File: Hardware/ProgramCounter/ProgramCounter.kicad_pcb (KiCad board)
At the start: 4 copper layers, 25 parts, among them J1 Conn_02x16_Counter_Clockwise, J2 Conn_02x16_Counter_Clockwise

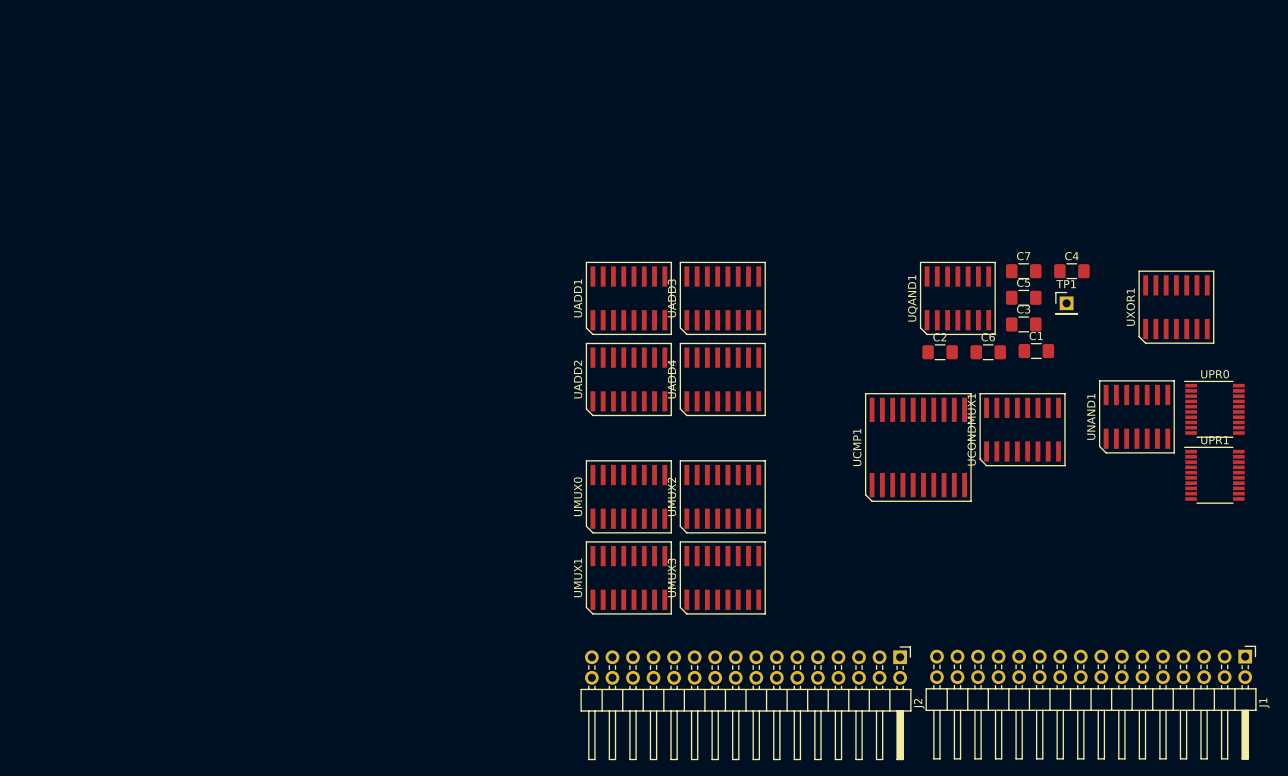
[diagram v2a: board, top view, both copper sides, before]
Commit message: PC Board
Mostly done. Going to move top half down.
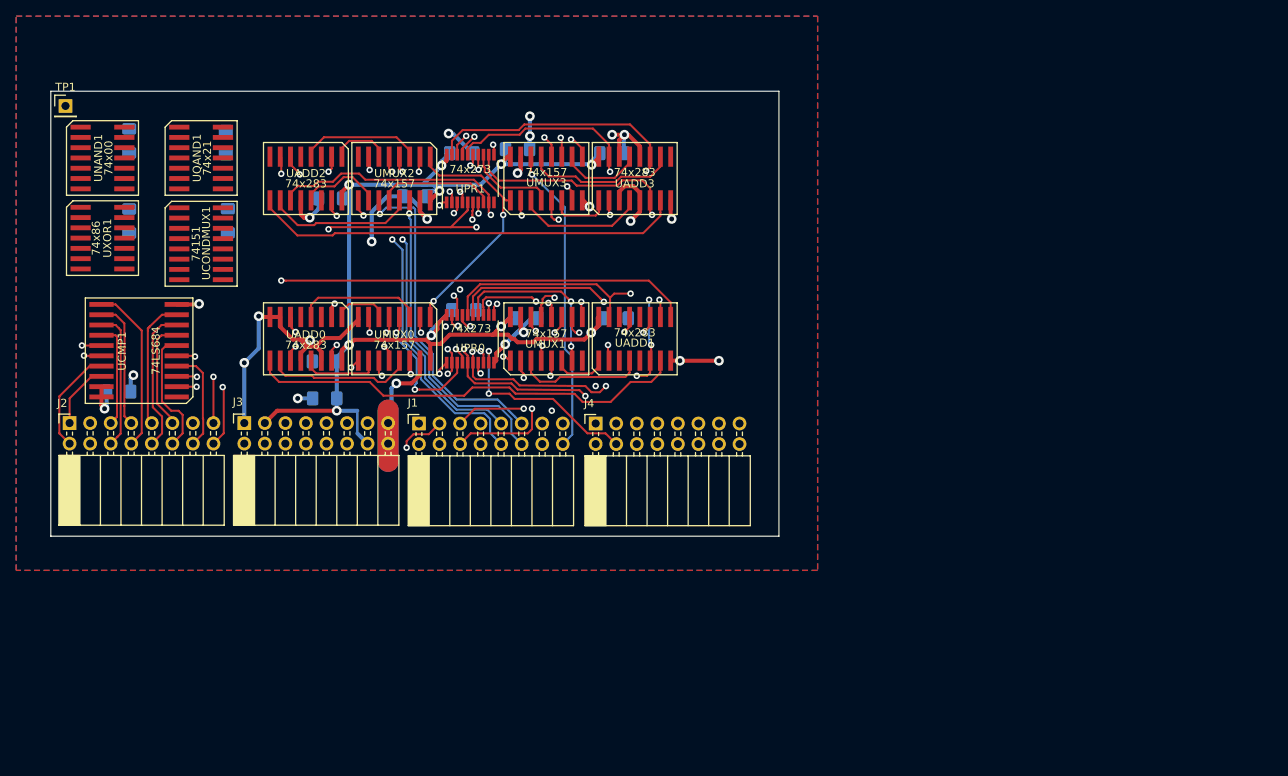
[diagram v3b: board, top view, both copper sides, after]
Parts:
- removed UADD4: 74LS283, aFootprint:R-PDSO-G16
- added C10: .1uF, Capacitor_SMD:C_1206_3216Metric_Pad1.42x1.75mm_HandSolder, B.Cu at (119.3, 57.7)
- added C11: .1uF, Capacitor_SMD:C_1206_3216Metric_Pad1.42x1.75mm_HandSolder, B.Cu at (84.6, 63.2)
- added C12: .1uF, Capacitor_SMD:C_1206_3216Metric_Pad1.42x1.75mm_HandSolder, B.Cu at (71.6, 56.4)
- added C13: .1uF, Capacitor_SMD:C_1206_3216Metric_Pad1.42x1.75mm_HandSolder, B.Cu at (59.7, 66.0)
- added C14: .1uF, Capacitor_SMD:C_1206_3216Metric_Pad1.42x1.75mm_HandSolder, B.Cu at (95.0, 63.0)
- added C15: .1uF, Capacitor_SMD:C_1206_3216Metric_Pad1.42x1.75mm_HandSolder, B.Cu at (107.7, 57.1)
- added C8: .1uF, Capacitor_SMD:C_1206_3216Metric_Pad1.42x1.75mm_HandSolder, B.Cu at (119.9, 78.1)
- added C9: .1uF, Capacitor_SMD:C_1206_3216Metric_Pad1.42x1.75mm_HandSolder, B.Cu at (83.9, 88.0)
- added J3: Conn_02x08, Connector_PinSocket_2.54mm:PinSocket_2x08_P2.54mm_Horizontal, F.Cu at (73.9, 91.0)
- added J4: Conn_02x08, Connector_PinSocket_2.54mm:PinSocket_2x08_P2.54mm_Horizontal, F.Cu at (117.3, 91.1)
- added UADD0: 74x283, aFootprint:R-PDSO-G16, F.Cu at (81.5, 80.6)
- C1, C2, C3, C4, C5, C6, C7: moved to B.Cu
- J1, J2: value Conn_02x16_Counter_Clockwise -> Conn_02x08; footprint Connector_PinHeader_2.54mm:PinHeader_2x16_P2.54mm_Horizontal -> Connector_PinSocket_2.54mm:PinSocket_2x08_P2.54mm_Horizontal
- UADD1, UADD2, UADD3: value 74LS283 -> 74x283
- UMUX0, UMUX1, UMUX2, UMUX3: value 74LS157 -> 74x157
- UNAND1: value 74LS00 -> 74x00
- UPR0, UPR1: value 74HCT273 -> 74x273
- UQAND1: value 74LS21 -> 74x21
- UXOR1: value 74HC86 -> 74x86
- moved UXOR1 133.0 mm to (56.4, 68.2), turned to 270 degrees
- moved UNAND1 131.8 mm to (56.4, 58.2), turned to 270 degrees
- moved TP1 126.1 mm to (51.8, 51.8)
- moved C4 117.6 mm to (59.7, 56.1), turned to 270 degrees
- moved C5 112.5 mm to (58.4, 87.1)
- moved J2 106.7 mm to (52.3, 91.0), turned to 90 degrees
- moved J1 106.1 mm to (95.5, 91.1), turned to 90 degrees
- moved UCONDMUX1 104.1 mm to (68.6, 68.8), turned to 270 degrees
- moved C3 99.2 mm to (71.9, 66.0), turned to 270 degrees
- moved UPR1 99.1 mm to (101.9, 60.8), turned to 90 degrees
- moved UCMP1 97.1 mm to (60.9, 82.1), turned to 90 degrees
- moved UQAND1 95.1 mm to (68.6, 58.2), turned to 270 degrees
- moved UPR0 92.5 mm to (101.9, 80.6), turned to 90 degrees
- moved C1 88.0 mm to (83.8, 83.4), turned to 180 degrees
- moved C7 71.0 mm to (100.8, 57.7)
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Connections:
- net Net-(UADD1-Pad9) renamed /16 Bit Adder/CARRY1
- net Net-(UADD2-Pad9) renamed /16 Bit Adder/CARRY2
- J1 pad 1: VCC -> /REGMEM0
- J1 pad 10: /RCS2 -> /REGMEM9
- J1 pad 11: /RCS1 -> /REGMEM10
- J1 pad 12: /RCS0 -> /REGMEM11
- J1 pad 13: /OPCODE3 -> /REGMEM12
- J1 pad 14: /OPCODE2 -> /REGMEM13
- J1 pad 15: /OPCODE1 -> /REGMEM14
- J1 pad 16: /OPCODE0 -> /REGMEM15
- J1 pad 2: GND -> /REGMEM1
- J1 pad 3: GND -> /REGMEM2
- J1 pad 4: /FLAG_CARRY -> /REGMEM3
- J1 pad 5: /RCS7 -> /REGMEM4
- J1 pad 6: /RCS6 -> /REGMEM7
- J1 pad 7: /RCS5 -> /REGMEM6
- J1 pad 8: /RCS4 -> /REGMEM5
- J1 pad 9: /RCS3 -> /REGMEM8
- J2 pad 1: /IMM0 -> /RCD7
- J2 pad 10: /RCD5 -> /RCS3
- J2 pad 11: /RCD6 -> /RCD2
- J2 pad 12: /RCD7 -> /RCS2
- J2 pad 13: /~RST -> /RCD1
- J2 pad 14: /CLK_WB -> /RCS1
- J2 pad 15: GND -> /RCD0
- J2 pad 16: VCC -> /RCS0
- J2 pad 2: /IMM1 -> /RCS7
- J2 pad 3: /IMM2 -> /RCD6
- J2 pad 4: /IMM3 -> /RCS6
- J2 pad 5: /RCD0 -> /RCD5
- J2 pad 6: /RCD1 -> /RCS5
- J2 pad 7: /RCD2 -> /RCD4
- J2 pad 8: /RCD3 -> /RCS4
- J2 pad 9: /RCD4 -> /RCD3
- UADD1 pad 1: /16 Bit Adder/COUT1 -> /16 Bit Adder/COUT5
- UADD1 pad 10: /16 Bit Adder/COUT3 -> /16 Bit Adder/COUT7
- UADD1 pad 11: /PCOUT3 -> /PCOUT7
- UADD1 pad 13: /16 Bit Adder/COUT2 -> /16 Bit Adder/COUT6
- UADD1 pad 15: /PCOUT2 -> /PCOUT6
- UADD1 pad 2: /PCOUT1 -> /PCOUT5
- UADD1 pad 3: /IS_SKIP -> GND
- UADD1 pad 4: /16 Bit Adder/COUT0 -> /16 Bit Adder/COUT4
- UADD1 pad 5: /~IS_SKIP -> GND
- UADD1 pad 6: /PCOUT0 -> /PCOUT4
- UADD1 pad 7: GND -> /16 Bit Adder/CARRY0
- UADD2 pad 1: /16 Bit Adder/COUT5 -> /16 Bit Adder/COUT9
- UADD2 pad 10: /16 Bit Adder/COUT7 -> /16 Bit Adder/COUT11
- UADD2 pad 11: /PCOUT7 -> /PCOUT11
- UADD2 pad 13: /16 Bit Adder/COUT6 -> /16 Bit Adder/COUT10
- UADD2 pad 15: /PCOUT6 -> /PCOUT10
- UADD2 pad 2: /PCOUT5 -> /PCOUT9
- UADD2 pad 4: /16 Bit Adder/COUT4 -> /16 Bit Adder/COUT8
- UADD2 pad 6: /PCOUT4 -> /PCOUT8
- UADD3 pad 1: /16 Bit Adder/COUT9 -> /16 Bit Adder/COUT13
- UADD3 pad 10: /16 Bit Adder/COUT11 -> /16 Bit Adder/COUT15
- UADD3 pad 11: /PCOUT11 -> /PCOUT15
- UADD3 pad 13: /16 Bit Adder/COUT10 -> /16 Bit Adder/COUT14
- UADD3 pad 15: /PCOUT10 -> /PCOUT14
- UADD3 pad 2: /PCOUT9 -> /PCOUT13
- UADD3 pad 4: /16 Bit Adder/COUT8 -> /16 Bit Adder/COUT12
- UADD3 pad 6: /PCOUT8 -> /PCOUT12
- UADD3 pad 9: Net-(UADD3-Pad9) -> /16 Bit Adder/COUNTCARRY
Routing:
- net VCC: track 0.00 -> 180.8 mm, vias 0 -> 11
- net GND: track 0.00 -> 147.9 mm, vias 0 -> 23
- net /PCOUT11: track 0.00 -> 81.1 mm, vias 0 -> 1
- net /PCOUT8: track 0.00 -> 81.0 mm, vias 0 -> 2
- net /PCOUT9: track 0.00 -> 77.5 mm, vias 0 -> 3
- net /PCOUT15: track 0.00 -> 71.1 mm, vias 0 -> 1
- net /PCOUT10: track 0.00 -> 68.0 mm, vias 0 -> 2
- net /PCOUT12: track 0.00 -> 67.5 mm, vias 0 -> 1
- net /16 Bit Adder/CARRY1: track 0.00 -> 66.4 mm, vias 0 -> 2
- net /PCOUT14: track 0.00 -> 61.3 mm, vias 0 -> 1
- net /CLK_WB: track 0.00 -> 59.4 mm, vias 0 -> 2
- net /PCOUT13: track 0.00 -> 57.4 mm, vias 0 -> 2
- net /16 Bit Adder/CARRY0: track 0.00 -> 55.3 mm
- net /16 Bit Adder/CARRY2: track 0.00 -> 53.5 mm
- net /PCOUT3: track 0.00 -> 52.5 mm, vias 0 -> 3
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- added copper zone on B.Cu, net GND
- added copper zone on F.Cu, net GND
- added copper zone on In1.Cu, net GND
- added copper zone on In2.Cu, net GND
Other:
- board outline added: 90 x 55 mm
- net class Power added: clearance 0.2, trace_width 0.5, via_dia 1.2, via_drill 0.6

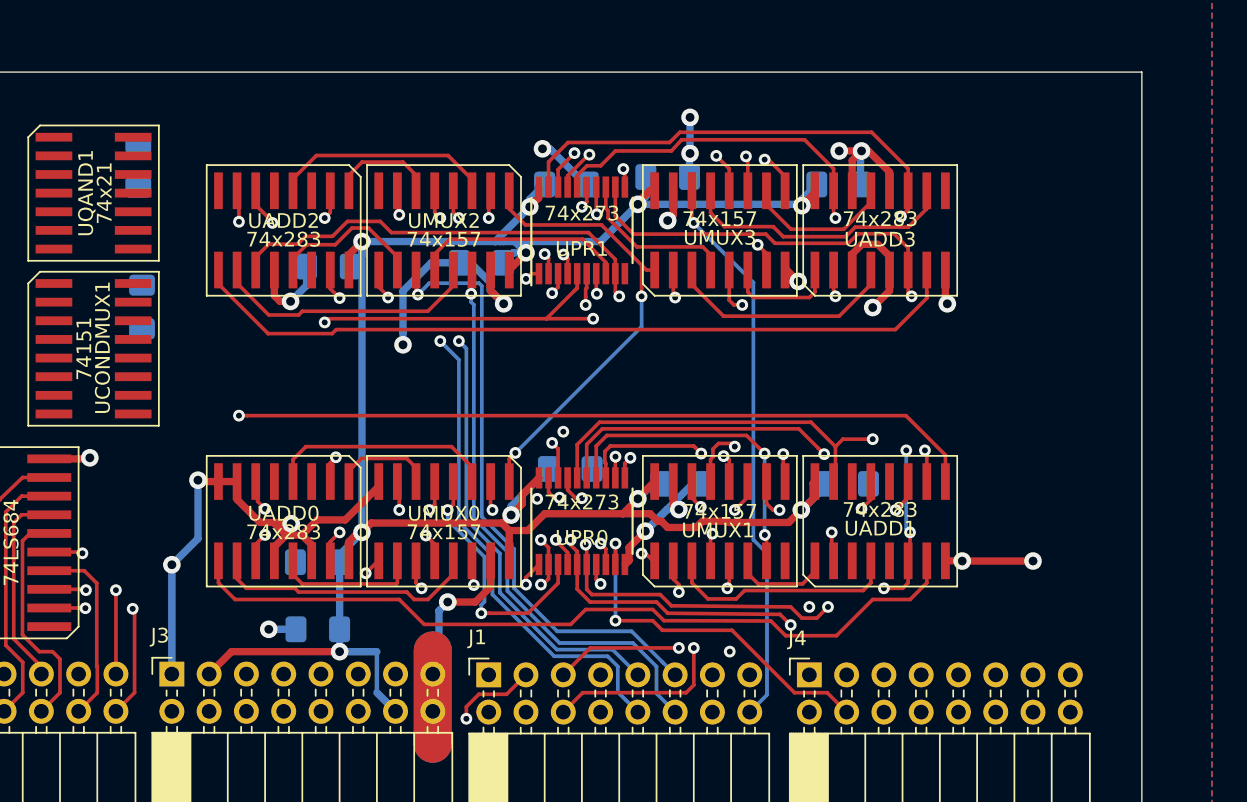
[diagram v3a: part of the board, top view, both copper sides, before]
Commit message: PC Board
Mostly done. Going to move register to the right and connect logic gates
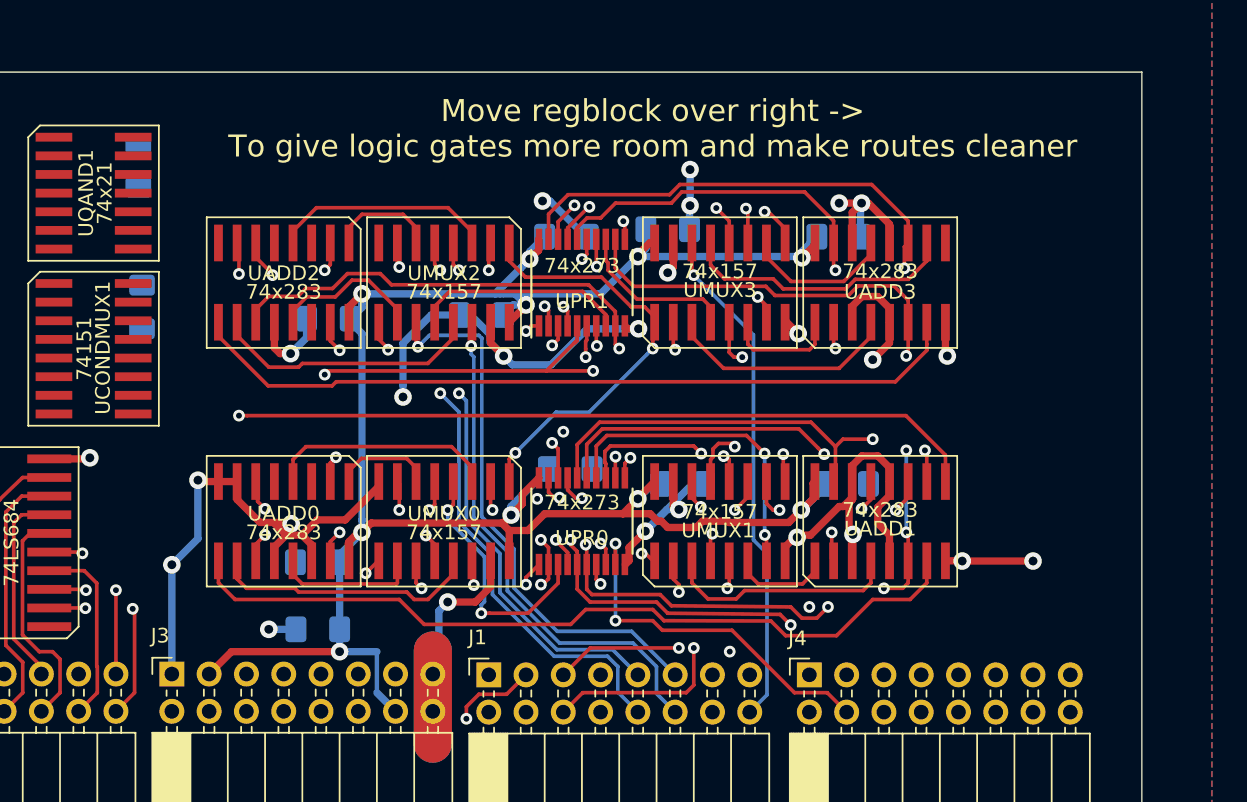
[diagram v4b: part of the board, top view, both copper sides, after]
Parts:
- moved C11 3.56 mm to (84.6, 66.8)
- moved C14 3.56 mm to (95.0, 66.5)
- moved C15 3.56 mm to (107.7, 60.7)
- moved C10 3.56 mm to (119.3, 61.2)
- moved C7 3.56 mm to (100.8, 61.2)
- moved UADD2 3.56 mm to (81.5, 64.3)
- moved UADD3 3.56 mm to (122.2, 64.3)
- moved UMUX2 3.56 mm to (92.5, 64.3)
- moved UMUX3 3.56 mm to (111.3, 64.3)
- moved UPR1 3.56 mm to (101.9, 64.3)
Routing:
- net GND: track 147.9 -> 184.7 mm, vias 23 -> 26
- net /PCOUT12: track 67.5 -> 59.4 mm
- net VCC: track 180.8 -> 175.9 mm
- net /REGMEM10: track 41.4 -> 37.8 mm
- net /~RST: track 39.8 -> 36.3 mm
- net /REGMEM14: track 38.7 -> 35.1 mm
- net /REGMEM13: track 34.1 -> 30.5 mm
- net /REGMEM15: track 38.1 -> 34.6 mm
- net /16 Bit Adder/CARRY1: track 66.4 -> 62.9 mm
- net /REGMEM9: track 43.4 -> 39.8 mm
- net /REGMEM8: track 41.2 -> 37.6 mm
- net /REGMEM11: track 38.8 -> 35.3 mm
- net /CLK_WB: track 59.4 -> 55.9 mm
- net /REGMEM12: track 29.3 -> 25.8 mm
- net /PCOUT15: track 71.1 -> 67.7 mm
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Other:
- board text added: "Move regblock over right -> To give logic gates more room and make routes cleaner"
